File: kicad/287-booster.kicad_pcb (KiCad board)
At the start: 2 copper layers, 24.9 x 51.6 mm, 5 parts, among them J1 Conn_01x02_Female, U1 80287, U2 Socket

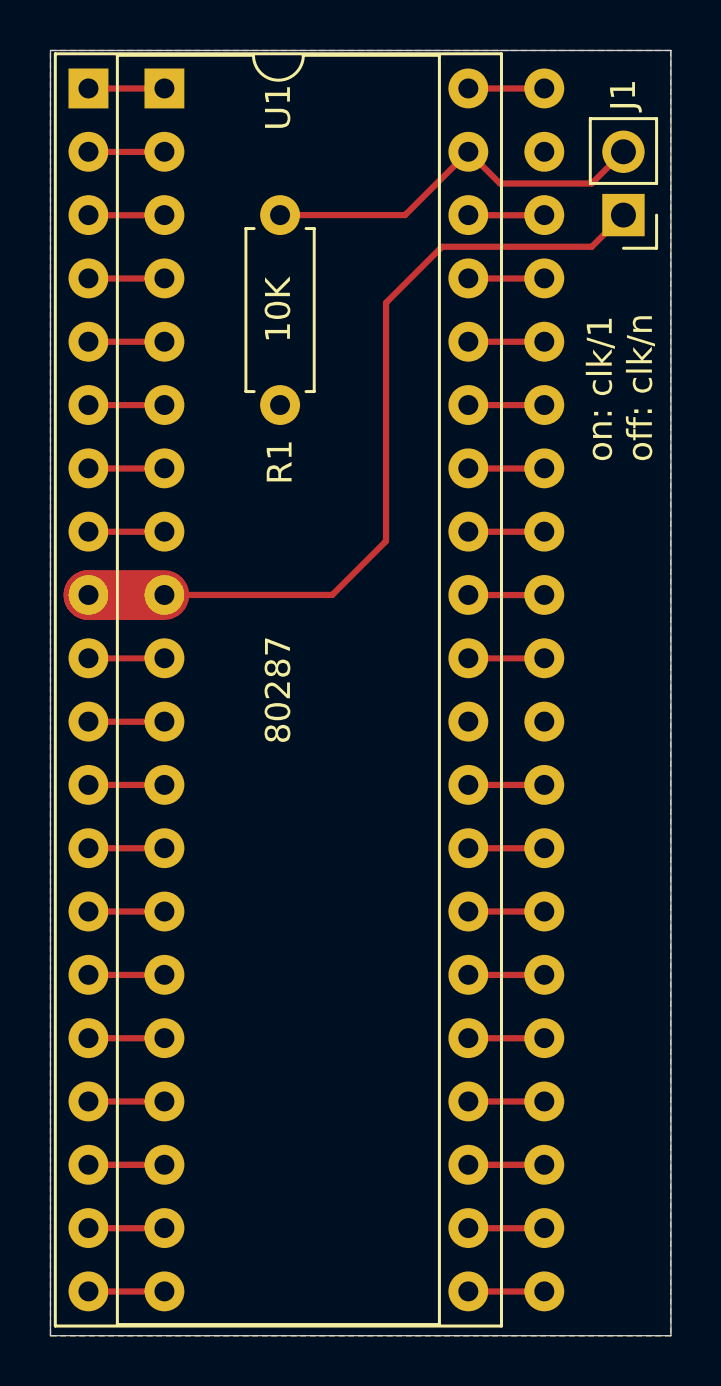
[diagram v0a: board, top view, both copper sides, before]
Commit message: Switched to KiCad 7
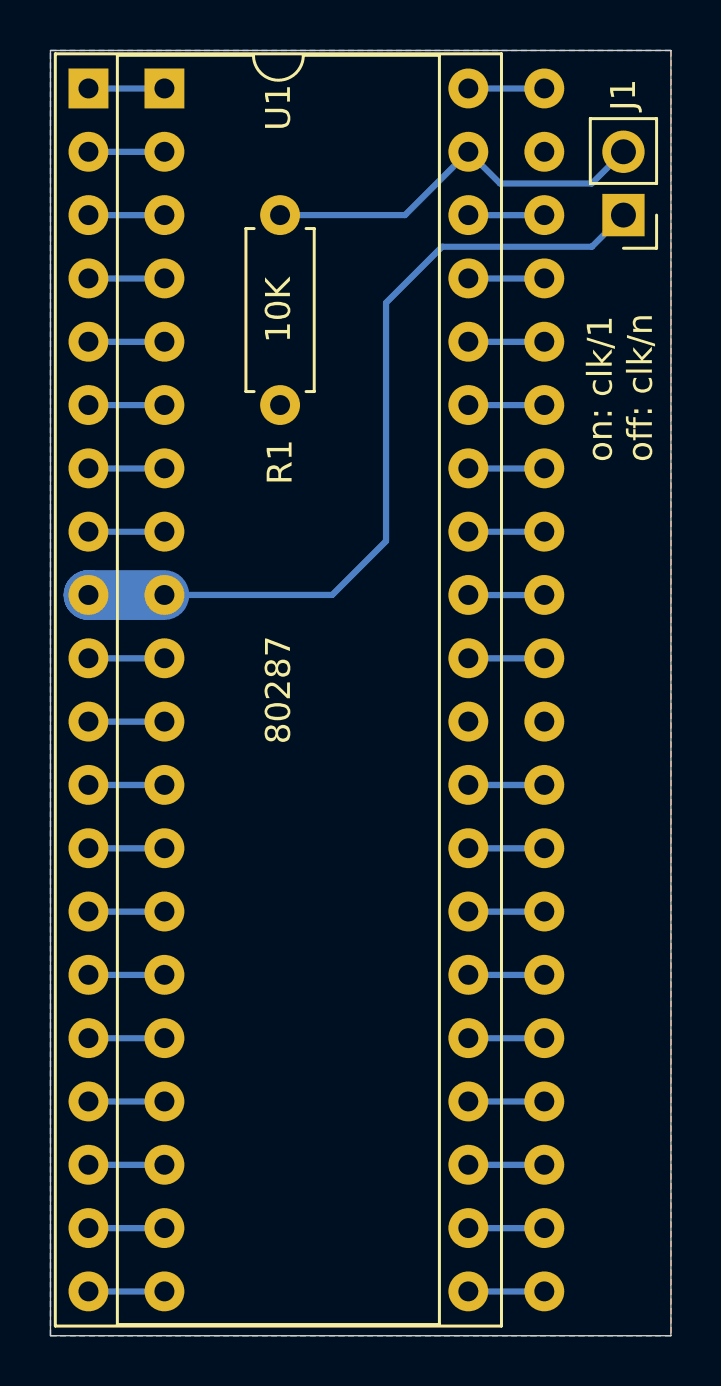
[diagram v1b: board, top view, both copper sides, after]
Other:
- board text added: "rev.${REVISION}"
- board text removed: "rev.1"
